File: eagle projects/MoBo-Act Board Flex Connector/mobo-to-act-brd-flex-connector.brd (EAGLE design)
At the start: 33 x 90.2 mm, 2 parts

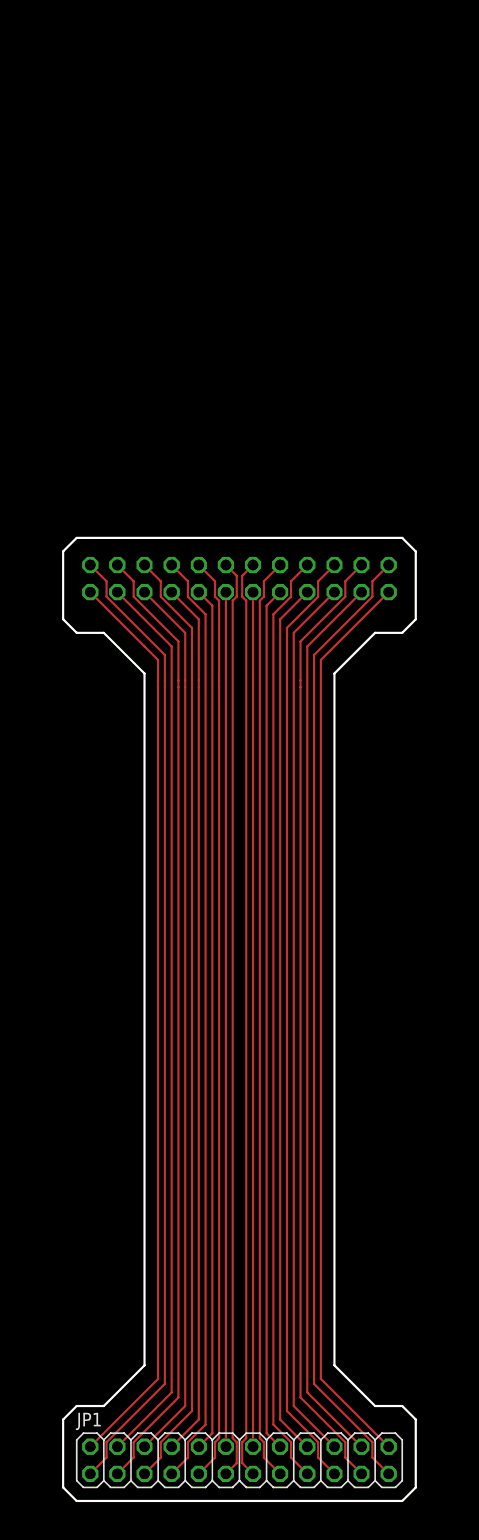
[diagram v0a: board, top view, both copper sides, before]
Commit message: Added mounting holes for M2 screws
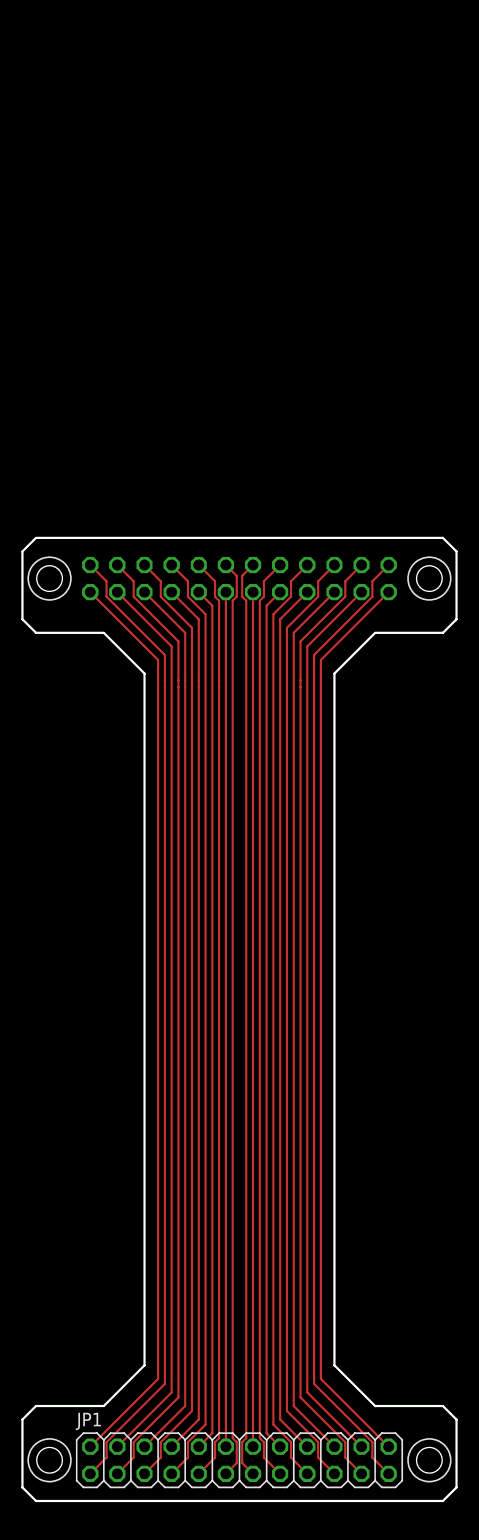
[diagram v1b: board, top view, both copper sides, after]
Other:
- board size 33 x 90.2 mm -> 40.6 x 90.2 mm
- board text added: "M2 screw clearance holes if required"
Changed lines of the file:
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@@
 <setting verticaltext="up"/>
 </settings>
-<grid distance="50" unitdist="mil" unit="mil" style="lines" multiple="1" display="yes" altdistance="25" altunitdist="mil" altunit="mil"/>
+<grid distance="50" unitdist="mil" unit="mm" style="lines" multiple="1" display="yes" altdistance="25" altunitdist="mil" altunit="mil"/>
 <layers>
 <layer number="1" name="Top" color="4" fill="1" visible="yes" active="yes"/>
@@
 <layer number="43" name="vRestrict" color="2" fill="10" visible="yes" active="yes"/>
 <layer number="44" name="Drills" color="7" fill="1" visible="no" active="yes"/>
-<layer number="45" name="Holes" color="7" fill="1" visible="no" active="yes"/>
+<layer number="45" name="Holes" color="7" fill="1" visible="yes" active="yes"/>
 <layer number="46" name="Milling" color="3" fill="1" visible="no" active="yes"/>
 <layer number="47" name="Measures" color="7" fill="1" visible="no" active="yes"/>
@@
 <board>
 <plain>
-<wire x1="14.1605" y1="13.97" x2="26.67" y2="13.97" width="0.1524" layer="48"/>
-<wire x1="26.67" y1="13.97" x2="39.1795" y2="13.97" width="0.1524" layer="48"/>
-<wire x1="13.97" y1="13.97" x2="11.43" y2="13.97" width="0.2032" layer="20"/>
-<wire x1="10.16" y1="12.7" x2="10.16" y2="6.35" width="0.2032" layer="20"/>
-<wire x1="10.16" y1="6.35" x2="11.43" y2="5.08" width="0.2032" layer="20"/>
-<wire x1="11.43" y1="5.08" x2="41.91" y2="5.08" width="0.2032" layer="20"/>
-<wire x1="41.91" y1="5.08" x2="43.18" y2="6.35" width="0.2032" layer="20"/>
-<wire x1="43.18" y1="6.35" x2="43.18" y2="12.7" width="0.2032" layer="20"/>
-<wire x1="43.18" y1="12.7" x2="41.91" y2="13.97" width="0.2032" layer="20"/>
-<wire x1="41.91" y1="13.97" x2="39.37" y2="13.97" width="0.2032" layer="20"/>
-<wire x1="10.16" y1="12.7" x2="11.43" y2="13.97" width="0.2032" layer="20"/>
+<wire x1="14.1605" y1="13.97" x2="39.1795" y2="13.97" width="0.1524" layer="48"/>
+<wire x1="13.97" y1="13.97" x2="7.62" y2="13.97" width="0.2032" layer="20"/>
+<wire x1="6.35" y1="12.7" x2="6.35" y2="6.35" width="0.2032" layer="20"/>
+<wire x1="6.35" y1="6.35" x2="7.62" y2="5.08" width="0.2032" layer="20"/>
+<wire x1="7.62" y1="5.08" x2="45.72" y2="5.08" width="0.2032" layer="20"/>
+<wire x1="45.72" y1="5.08" x2="46.99" y2="6.35" width="0.2032" layer="20"/>
+<wire x1="46.99" y1="6.35" x2="46.99" y2="12.7" width="0.2032" layer="20"/>
+<wire x1="46.99" y1="12.7" x2="45.72" y2="13.97" width="0.2032" layer="20"/>
+<wire x1="45.72" y1="13.97" x2="39.37" y2="13.97" width="0.2032" layer="20"/>
+<wire x1="6.35" y1="12.7" x2="7.62" y2="13.97" width="0.2032" layer="20"/>
 <wire x1="17.78" y1="17.78" x2="17.78" y2="82.55" width="0.2032" layer="20"/>
 <wire x1="35.56" y1="17.78" x2="35.56" y2="82.55" width="0.2032" layer="20"/>
-<wire x1="43.18" y1="93.98" x2="43.18" y2="87.63" width="0.2032" layer="20"/>
-<wire x1="43.18" y1="87.63" x2="41.91" y2="86.36" width="0.2032" layer="20"/>
-<wire x1="41.91" y1="86.36" x2="39.37" y2="86.36" width="0.2032" layer="20"/>
-<wire x1="43.18" y1="93.98" x2="41.91" y2="95.25" width="0.2032" layer="20"/>
-<wire x1="41.91" y1="95.25" x2="11.43" y2="95.25" width="0.2032" layer="20"/>
-<wire x1="11.43" y1="95.25" x2="10.16" y2="93.98" width="0.2032" layer="20"/>
-<wire x1="10.16" y1="93.98" x2="10.16" y2="87.63" width="0.2032" layer="20"/>
-<wire x1="10.16" y1="87.63" x2="11.43" y2="86.36" width="0.2032" layer="20"/>
-<wire x1="11.43" y1="86.36" x2="13.97" y2="86.36" width="0.2032" layer="20"/>
+<wire x1="46.99" y1="93.98" x2="46.99" y2="87.63" width="0.2032" layer="20"/>
+<wire x1="46.99" y1="87.63" x2="45.72" y2="86.36" width="0.2032" layer="20"/>
+<wire x1="45.72" y1="86.36" x2="39.37" y2="86.36" width="0.2032" layer="20"/>
+<wire x1="46.99" y1="93.98" x2="45.72" y2="95.25" width="0.2032" layer="20"/>
+<wire x1="45.72" y1="95.25" x2="7.62" y2="95.25" width="0.2032" layer="20"/>
+<wire x1="7.62" y1="95.25" x2="6.35" y2="93.98" width="0.2032" layer="20"/>
+<wire x1="6.35" y1="93.98" x2="6.35" y2="87.63" width="0.2032" layer="20"/>
+<wire x1="6.35" y1="87.63" x2="7.62" y2="86.36" width="0.2032" layer="20"/>
+<wire x1="7.62" y1="86.36" x2="13.97" y2="86.36" width="0.2032" layer="20"/>
 <wire x1="13.97" y1="86.36" x2="17.78" y2="82.55" width="0.2032" layer="20"/>
 <wire x1="35.56" y1="82.55" x2="39.37" y2="86.36" width="0.2032" layer="20"/>
@@
 <wire x1="39.37" y1="13.97" x2="35.56" y2="17.78" width="0.2032" layer="20"/>
 <dimension x1="43.18" y1="13.97" x2="43.18" y2="86.36" x3="52.07" y3="50.165" textsize="1.778" layer="20"/>
+<hole x="8.89" y="8.89" drill="2.4"/>
+<circle x="8.89" y="8.89" radius="2" width="0.1524" layer="21"/>
+<hole x="44.45" y="8.89" drill="2.4"/>
+<circle x="44.45" y="8.89" radius="2" width="0.1524" layer="21"/>
+<hole x="8.89" y="91.44" drill="2.4"/>
+<circle x="8.89" y="91.44" radius="2" width="0.1524" layer="21"/>
+<hole x="44.45" y="91.44" drill="2.4"/>
+<circle x="44.45" y="91.44" radius="2" width="0.1524" layer="21"/>
+<text x="6.35" y="1.27" size="1.778" layer="48">M2 screw clearance holes if required</text>
 </plain>
 <attributes>

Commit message: Added 24 pin SMD header and lengthened both connectors
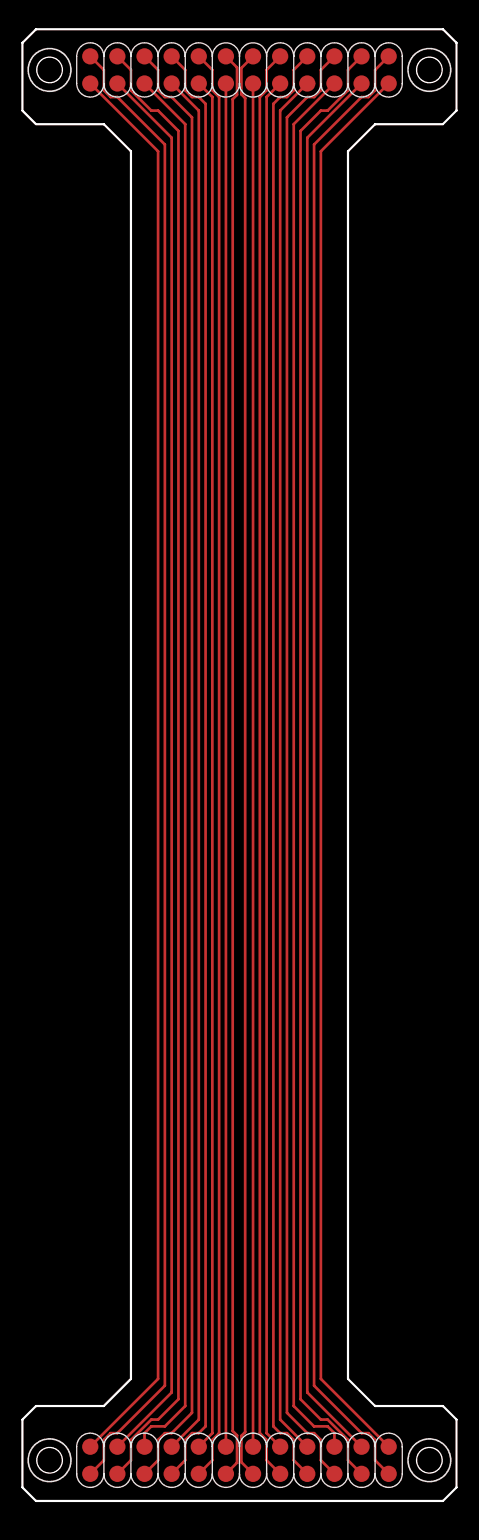
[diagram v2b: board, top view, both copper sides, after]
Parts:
- removed JP1, JP2: (no value), pinhead:2X12
- added U$1, U$2: 12X2_SMD_2.54MM_HEADER, SMD_headers:12X2_HEADER
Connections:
- net N$1: now also U$1.X1, U$2.X24; no longer JP1.2, JP2.2
- net N$10: now also U$1.X10, U$2.X15; no longer JP1.20, JP2.20
- net N$11: now also U$1.X11, U$2.X14; no longer JP1.22, JP2.22
- net N$12: now also U$1.X12, U$2.X13; no longer JP1.24, JP2.24
- net N$13: now also U$1.X24, U$2.X1; no longer JP1.1, JP2.1
- net N$14: now also U$1.X23, U$2.X2; no longer JP1.3, JP2.3
- net N$15: now also U$1.X22, U$2.X3; no longer JP1.5, JP2.5
- net N$16: now also U$1.X21, U$2.X4; no longer JP1.7, JP2.7
- net N$17: now also U$1.X20, U$2.X5; no longer JP1.9, JP2.9
- net N$18: now also U$1.X19, U$2.X6; no longer JP1.11, JP2.11
- net N$19: now also U$1.X18, U$2.X7; no longer JP1.13, JP2.13
- net N$2: now also U$1.X2, U$2.X23; no longer JP1.4, JP2.4
- net N$20: now also U$1.X17, U$2.X8; no longer JP1.15, JP2.15
- net N$21: now also U$1.X16, U$2.X9; no longer JP1.17, JP2.17
- net N$22: now also U$1.X15, U$2.X10; no longer JP1.19, JP2.19
- net N$23: now also U$1.X14, U$2.X11; no longer JP1.21, JP2.21
- net N$24: now also U$1.X13, U$2.X12; no longer JP1.23, JP2.23
- net N$3: now also U$1.X3, U$2.X22; no longer JP1.6, JP2.6
- net N$4: now also U$1.X4, U$2.X21; no longer JP1.8, JP2.8
- net N$5: now also U$1.X5, U$2.X20; no longer JP1.10, JP2.10
- net N$6: now also U$1.X6, U$2.X19; no longer JP1.12, JP2.12
- net N$7: now also U$1.X7, U$2.X18; no longer JP1.14, JP2.14
- net N$8: now also U$1.X8, U$2.X17; no longer JP1.16, JP2.16
- net N$9: now also U$1.X9, U$2.X16; no longer JP1.18, JP2.18
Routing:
- net N$2: track 84.2 -> 138.2 mm
- net N$12: track 85.3 -> 139.2 mm
- net N$9: track 82.1 -> 136.1 mm
- net N$4: track 82.1 -> 136.1 mm
- net N$3: track 83.2 -> 137.1 mm
- net N$10: track 83.2 -> 137.1 mm
- net N$1: track 85.3 -> 139.2 mm
- net N$11: track 84.2 -> 138.2 mm
- net N$6: track 80.0 -> 133.9 mm
- net N$7: track 80.0 -> 133.9 mm
- net N$8: track 81.1 -> 134.3 mm
- net N$5: track 81.1 -> 134.3 mm
- net N$22: track 88.8 -> 131.5 mm
- net N$15: track 88.8 -> 131.5 mm
- net N$16: track 87.7 -> 130.4 mm
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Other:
- board size 40.6 x 90.2 mm -> 40.6 x 137.8 mm

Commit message: Added stiffener polygons
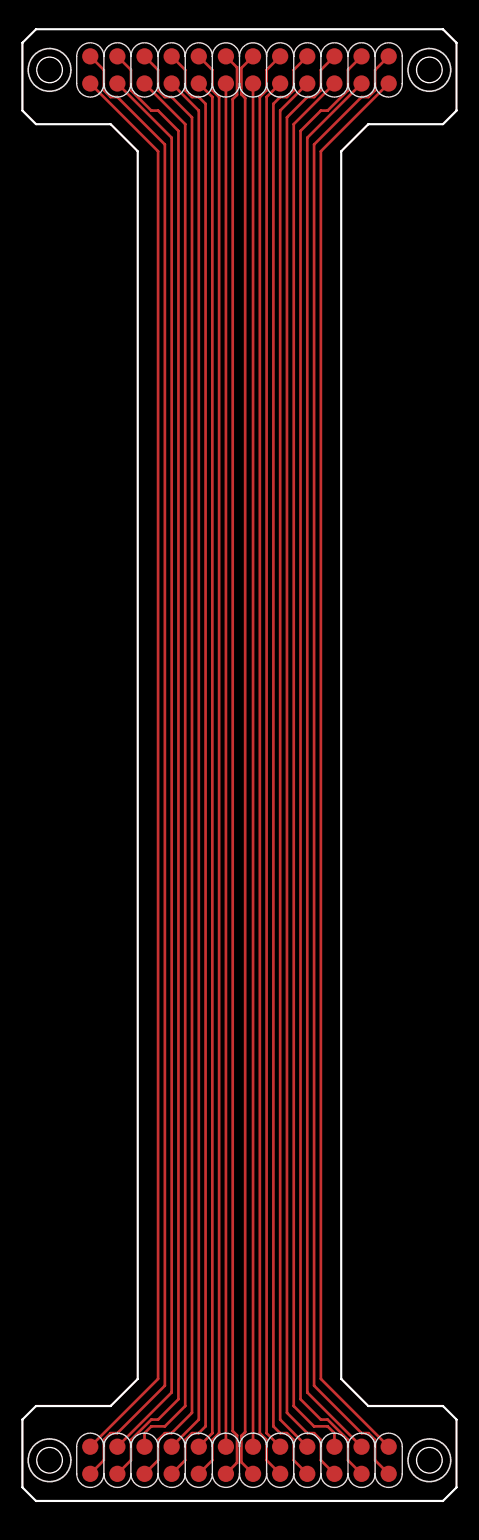
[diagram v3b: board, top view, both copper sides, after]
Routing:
- net N$16: track 130.4 -> 129.7 mm
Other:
- outline, holes or cut-outs redrawn
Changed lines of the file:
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@@
 <board>
 <plain>
-<wire x1="13.97" y1="13.97" x2="7.62" y2="13.97" width="0.2032" layer="20"/>
+<wire x1="14.605" y1="13.97" x2="7.62" y2="13.97" width="0.2032" layer="20"/>
 <wire x1="6.35" y1="12.7" x2="6.35" y2="6.35" width="0.2032" layer="20"/>
 <wire x1="6.35" y1="6.35" x2="7.62" y2="5.08" width="0.2032" layer="20"/>
@@
 <wire x1="46.99" y1="6.35" x2="46.99" y2="12.7" width="0.2032" layer="20"/>
 <wire x1="46.99" y1="12.7" x2="45.72" y2="13.97" width="0.2032" layer="20"/>
-<wire x1="45.72" y1="13.97" x2="39.37" y2="13.97" width="0.2032" layer="20"/>
+<wire x1="45.72" y1="13.97" x2="38.735" y2="13.97" width="0.2032" layer="20"/>
 <wire x1="6.35" y1="12.7" x2="7.62" y2="13.97" width="0.2032" layer="20"/>
-<wire x1="16.51" y1="16.51" x2="16.51" y2="131.445" width="0.2032" layer="20"/>
-<wire x1="36.83" y1="16.51" x2="36.83" y2="131.445" width="0.2032" layer="20"/>
+<wire x1="17.145" y1="16.51" x2="17.145" y2="131.445" width="0.2032" layer="20"/>
+<wire x1="36.195" y1="16.51" x2="36.195" y2="131.445" width="0.2032" layer="20"/>
 <wire x1="46.99" y1="141.605" x2="46.99" y2="135.255" width="0.2032" layer="20"/>
 <wire x1="46.99" y1="135.255" x2="45.72" y2="133.985" width="0.2032" layer="20"/>
-<wire x1="45.72" y1="133.985" x2="39.37" y2="133.985" width="0.2032" layer="20"/>
+<wire x1="45.72" y1="133.985" x2="38.735" y2="133.985" width="0.2032" layer="20"/>
 <wire x1="46.99" y1="141.605" x2="45.72" y2="142.875" width="0.2032" layer="20"/>
 <wire x1="45.72" y1="142.875" x2="7.62" y2="142.875" width="0.2032" layer="20"/>
@@
 <wire x1="6.35" y1="141.605" x2="6.35" y2="135.255" width="0.2032" layer="20"/>
 <wire x1="6.35" y1="135.255" x2="7.62" y2="133.985" width="0.2032" layer="20"/>
-<wire x1="7.62" y1="133.985" x2="13.97" y2="133.985" width="0.2032" layer="20"/>
-<wire x1="13.97" y1="133.985" x2="16.51" y2="131.445" width="0.2032" layer="20"/>
-<wire x1="36.83" y1="131.445" x2="39.37" y2="133.985" width="0.2032" layer="20"/>
-<wire x1="13.97" y1="13.97" x2="16.51" y2="16.51" width="0.2032" layer="20"/>
-<wire x1="39.37" y1="13.97" x2="36.83" y2="16.51" width="0.2032" layer="20"/>
+<wire x1="7.62" y1="133.985" x2="14.605" y2="133.985" width="0.2032" layer="20"/>
+<wire x1="14.605" y1="133.985" x2="17.145" y2="131.445" width="0.2032" layer="20"/>
+<wire x1="36.195" y1="131.445" x2="38.735" y2="133.985" width="0.2032" layer="20"/>
+<wire x1="14.605" y1="13.97" x2="17.145" y2="16.51" width="0.2032" layer="20"/>
+<wire x1="38.735" y1="13.97" x2="36.195" y2="16.51" width="0.2032" layer="20"/>
 <dimension x1="43.18" y1="13.97" x2="43.18" y2="133.985" x3="52.07" y3="73.9775" textsize="1.778" layer="20"/>
 <hole x="8.89" y="8.89" drill="2.4"/>
@@
 <circle x="44.45" y="139.065" radius="2" width="0.1524" layer="21"/>
 <text x="6.35" y="1.27" size="1.778" layer="48">M2 screw clearance holes if required</text>
+<polygon width="0.1524" layer="114">
+<vertex x="6.35" y="12.7"/>
+<vertex x="6.35" y="6.35"/>
+<vertex x="7.62" y="5.08"/>
+<vertex x="45.72" y="5.08"/>
+<vertex x="46.99" y="6.35"/>
+<vertex x="46.99" y="12.7"/>
+<vertex x="45.72" y="13.97"/>
+<vertex x="7.62" y="13.97"/>
+</polygon>
+<polygon width="0.1524" layer="114">
+<vertex x="6.35" y="135.255"/>
+<vertex x="6.35" y="141.605"/>
+<vertex x="7.62" y="142.875"/>
+<vertex x="45.72" y="142.875"/>
+<vertex x="46.99" y="141.605"/>
+<vertex x="46.99" y="135.255"/>
+<vertex x="45.72" y="133.985"/>
+<vertex x="7.62" y="133.985"/>
+</polygon>
 </plain>
 <attributes>
@@
 <wire x1="30.48" y1="12.7" x2="30.48" y2="135.255" width="0.254" layer="1"/>
 <wire x1="30.48" y1="135.255" x2="33.02" y2="137.795" width="0.254" layer="1"/>
-<wire x1="33.02" y1="137.795" x2="33.655" y2="137.795" width="0.254" layer="1"/>
 </signal>
 <signal name="N$17">
@@
 <contactref element="U$2" pad="X6"/>
 <contactref element="U$1" pad="X19"/>
-<wire x1="27.94" y1="137.795" x2="27.94" y2="10.16" width="0.254" layer="1"/>
-<wire x1="27.94" y1="137.795" x2="27.94" y2="10.16" width="0" layer="19"/>
-<wire x1="27.94" y1="137.795" x2="27.94" y2="10.16" width="0" layer="19"/>
-<wire x1="27.94" y1="137.795" x2="27.94" y2="10.16" width="0" layer="19"/>
-<wire x1="27.94" y1="137.795" x2="27.94" y2="10.16" width="0" layer="19"/>
+<wire x1="27.94" y1="10.16" x2="27.94" y2="137.795" width="0.254" layer="1"/>
 </signal>
 <signal name="N$19">
@@
 <contactref element="U$1" pad="X18"/>
 <wire x1="25.4" y1="10.16" x2="25.4" y2="137.795" width="0.254" layer="1"/>
-<wire x1="25.4" y1="10.16" x2="25.4" y2="137.795" width="0" layer="19"/>
-<wire x1="25.4" y1="10.16" x2="25.4" y2="137.795" width="0" layer="19"/>
-<wire x1="25.4" y1="10.16" x2="25.4" y2="137.795" width="0" layer="19"/>
-<wire x1="25.4" y1="10.16" x2="25.4" y2="137.795" width="0" layer="19"/>
 </signal>
 <signal name="N$20">

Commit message: Mirrored one of the connectors ends (incorrectly)
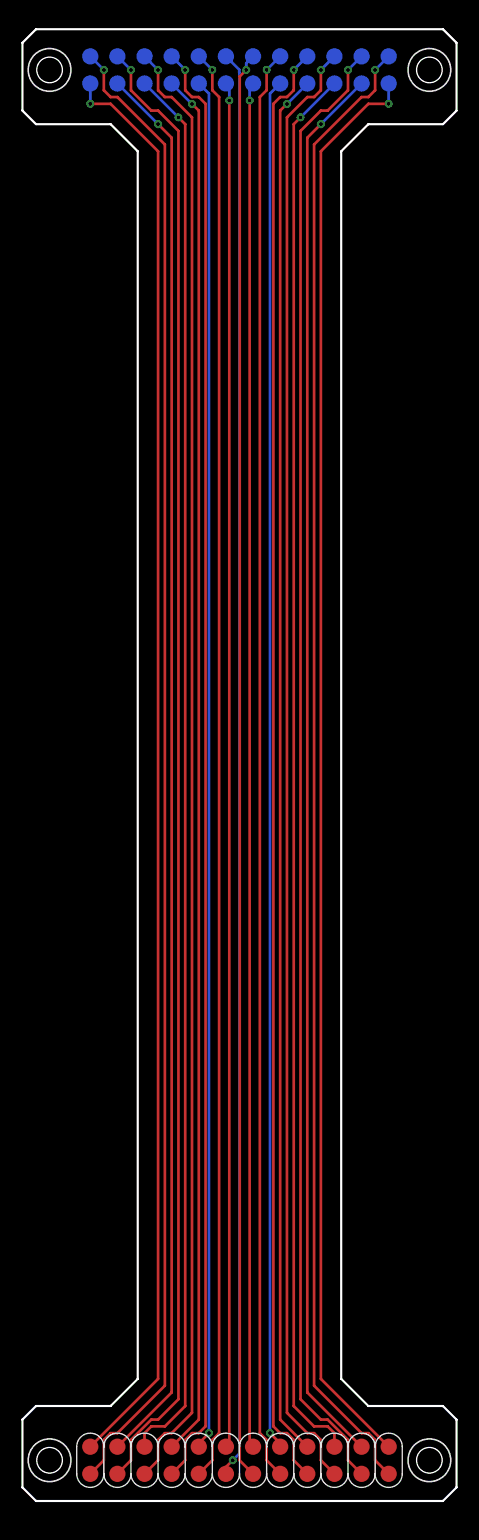
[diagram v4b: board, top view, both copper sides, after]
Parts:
- U$2: value 12X2_SMD_2.54MM_HEADER -> 12X2_MIRRORED_SMD_2.54MM_HEADER
- flipped U$2 to the bottom, turned to 180 degrees
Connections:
- net N$1: now also U$2.X1; no longer U$2.X24
- net N$10: now also U$2.X10; no longer U$2.X15
- net N$11: now also U$2.X11; no longer U$2.X14
- net N$12: now also U$2.X12; no longer U$2.X13
- net N$13: now also U$2.X24; no longer U$2.X1
- net N$14: now also U$2.X23; no longer U$2.X2
- net N$15: now also U$2.X22; no longer U$2.X3
- net N$16: now also U$2.X21; no longer U$2.X4
- net N$17: now also U$2.X20; no longer U$2.X5
- net N$18: now also U$2.X19; no longer U$2.X6
- net N$19: now also U$2.X18; no longer U$2.X7
- net N$2: now also U$2.X2; no longer U$2.X23
- net N$20: now also U$2.X17; no longer U$2.X8
- net N$21: now also U$2.X16; no longer U$2.X9
- net N$22: now also U$2.X15; no longer U$2.X10
- net N$23: now also U$2.X14; no longer U$2.X11
- net N$24: now also U$2.X13; no longer U$2.X12
- net N$3: now also U$2.X3; no longer U$2.X22
- net N$4: now also U$2.X4; no longer U$2.X21
- net N$5: now also U$2.X5; no longer U$2.X20
- net N$6: now also U$2.X6; no longer U$2.X19
- net N$7: now also U$2.X7; no longer U$2.X18
- net N$8: now also U$2.X8; no longer U$2.X17
- net N$9: now also U$2.X9; no longer U$2.X16
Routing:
- net N$24: track 132.9 -> 134.0 mm, vias 0 -> 1
- net N$13: track 132.9 -> 134.0 mm, vias 0 -> 1
- net N$20: track 128.7 -> 128.4 mm, vias 0 -> 1
- net N$19: track 127.6 -> 127.9 mm, vias 0 -> 1
- net N$18: track 127.6 -> 127.9 mm, vias 0 -> 1
- net N$17: track 128.7 -> 128.4 mm, vias 0 -> 1
- net N$6: track 133.9 -> 133.7 mm, vias 0 -> 1
- net N$7: track 133.9 -> 133.8 mm, vias 0 -> 1
- net N$21: track 129.7 -> 129.8 mm, vias 0 -> 1
- net N$16: track 129.7 -> 129.8 mm, vias 0 -> 1
- net N$22: vias 0 -> 1
- net N$9: vias 0 -> 1
- net N$8: vias 0 -> 1
- net N$5: vias 0 -> 1
- net N$4: vias 0 -> 1
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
